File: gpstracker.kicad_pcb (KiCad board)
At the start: 2 copper layers, 75.2 x 54.6 mm, 66 parts, among them IC1 SIM808, J1 Molex 47346-0001, J2 Leds, J3 47553-0001, J4 CONN_COAXIAL, J5 CONN_COAXIAL, J6 Micro_SD_Card, Q1 DMP1045U, SW1 Reset, U1 MCP73832-5-OT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

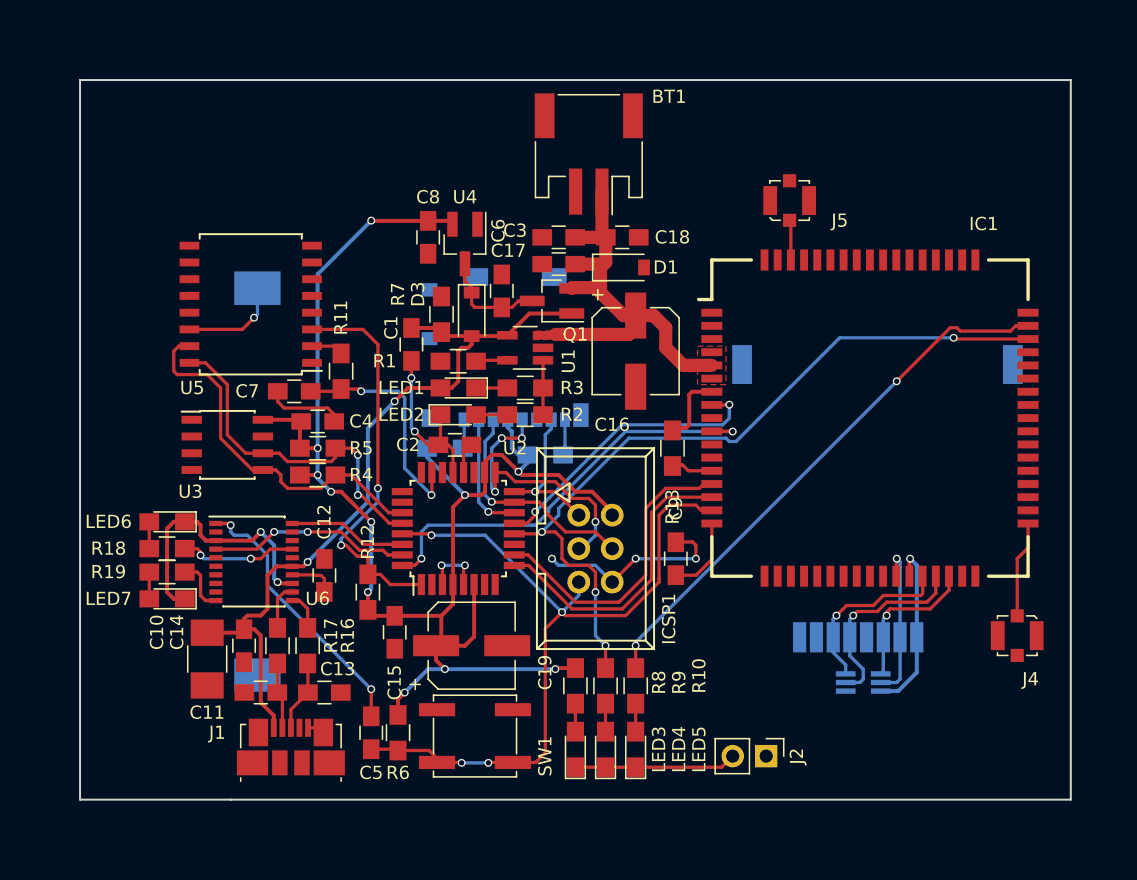
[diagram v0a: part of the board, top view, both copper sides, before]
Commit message: Finished PCB, powering eeprom from arduino
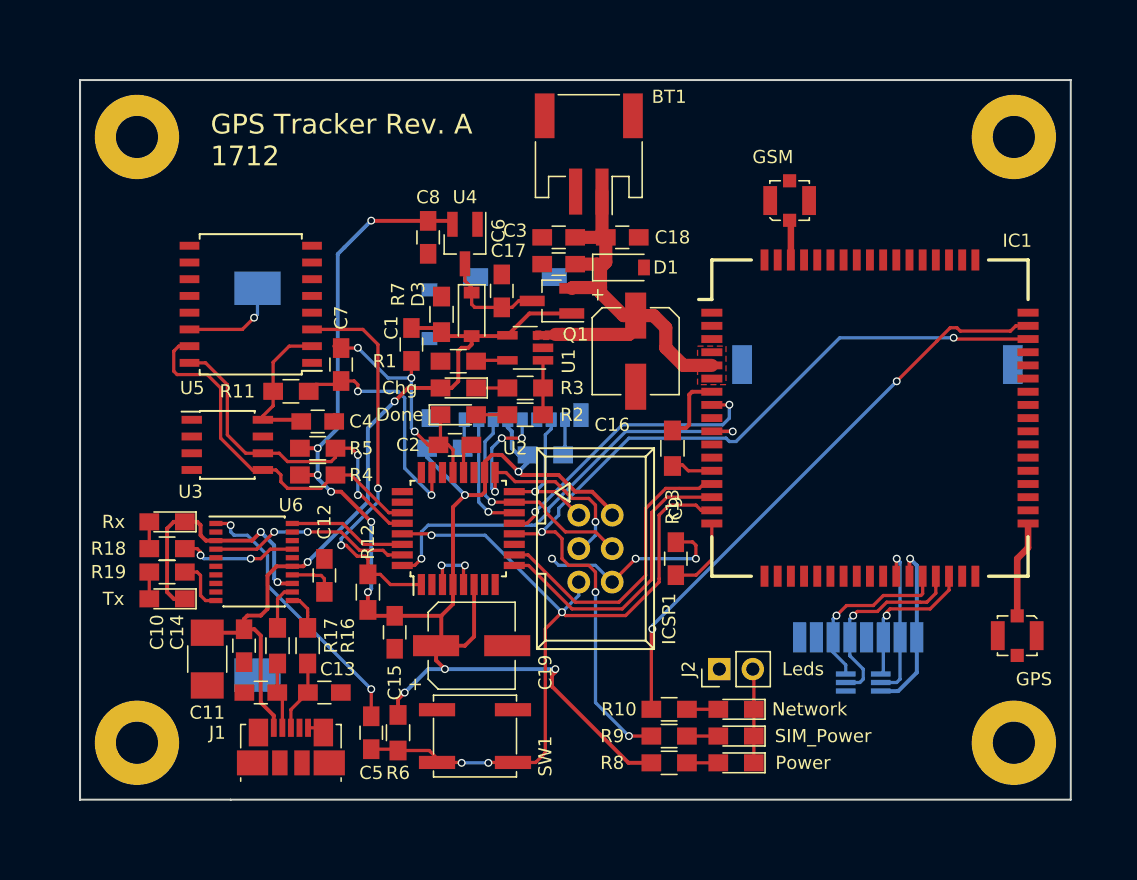
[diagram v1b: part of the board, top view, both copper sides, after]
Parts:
- added REF**: MountingHole_3.2mm_M3_Pad, Mounting_Holes:MountingHole_3.2mm_M3_Pad, F.Cu at (171.7, 118.9)
- added REF**: MountingHole_3.2mm_M3_Pad, Mounting_Holes:MountingHole_3.2mm_M3_Pad, F.Cu at (171.7, 72.9)
- added REF**: MountingHole_3.2mm_M3_Pad, Mounting_Holes:MountingHole_3.2mm_M3_Pad, F.Cu at (105.2, 118.9)
- added REF**: MountingHole_3.2mm_M3_Pad, Mounting_Holes:MountingHole_3.2mm_M3_Pad, F.Cu at (105.2, 72.9)
- moved LED3 12.2 mm to (150.6, 120.4), turned to 180 degrees
- moved LED4 9.96 mm to (150.6, 118.4), turned to 180 degrees
- moved R8 9.20 mm to (145.5, 120.4), turned to 180 degrees
- moved LED5 8.21 mm to (150.6, 116.3), turned to 180 degrees
- moved J2 7.50 mm to (149.4, 113.3), turned to 90 degrees
- moved R9 6.15 mm to (145.5, 118.4), turned to 180 degrees
- moved R11 4.10 mm to (116.8, 92.2), turned to 0 degrees
- moved C7 4.10 mm to (120.7, 90.2), turned to 90 degrees
- moved R10 3.10 mm to (145.5, 116.3), turned to 180 degrees
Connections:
- net Net-(IC1-Pad35) renamed /GPS
- net Net-(IC1-Pad66) renamed /GSM
- C4 pad 1: +3V3 -> +3.3VP
- R11 pad 1: Net-(R11-Pad1) -> +3.3VP
- U3 pad 8: +3V3 -> +3.3VP
- U5 pad 2: Net-(R11-Pad1) -> +3.3VP
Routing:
- net +3.3VP: track 0.00 -> 11.2 mm
- net /SIM808_S: track 59.5 -> 67.1 mm
- net Net-(J2-Pad2): track 12.3 -> 7.15 mm
- net +3V3: track 116.5 -> 121.3 mm
- net /NETWORK_LED: track 41.9 -> 44.5 mm
- net Net-(R11-Pad1): track 2.44 -> 0.00 mm
- net GND: track 52.3 -> 53.9 mm, vias 8 -> 9
- net /RTC_PWR: track 17.4 -> 18.3 mm
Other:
- net class RF added: clearance 0.2, trace_width 0.5, via_dia 0.6, via_drill 0.4
- board text added: "GPS"
- board text added: "GPS Tracker Rev. A 1712"
- board text added: "GSM"

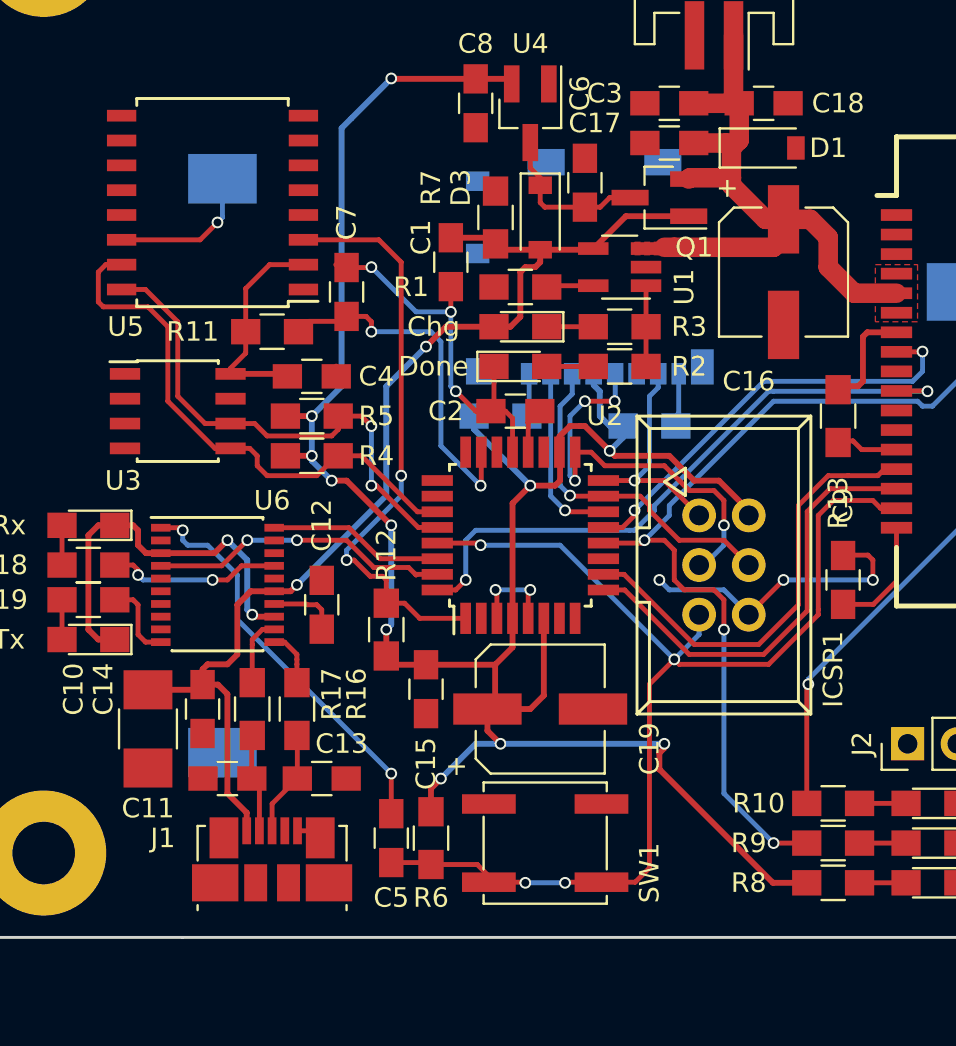
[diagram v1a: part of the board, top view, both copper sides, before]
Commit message: Added via near decoupling capacitors
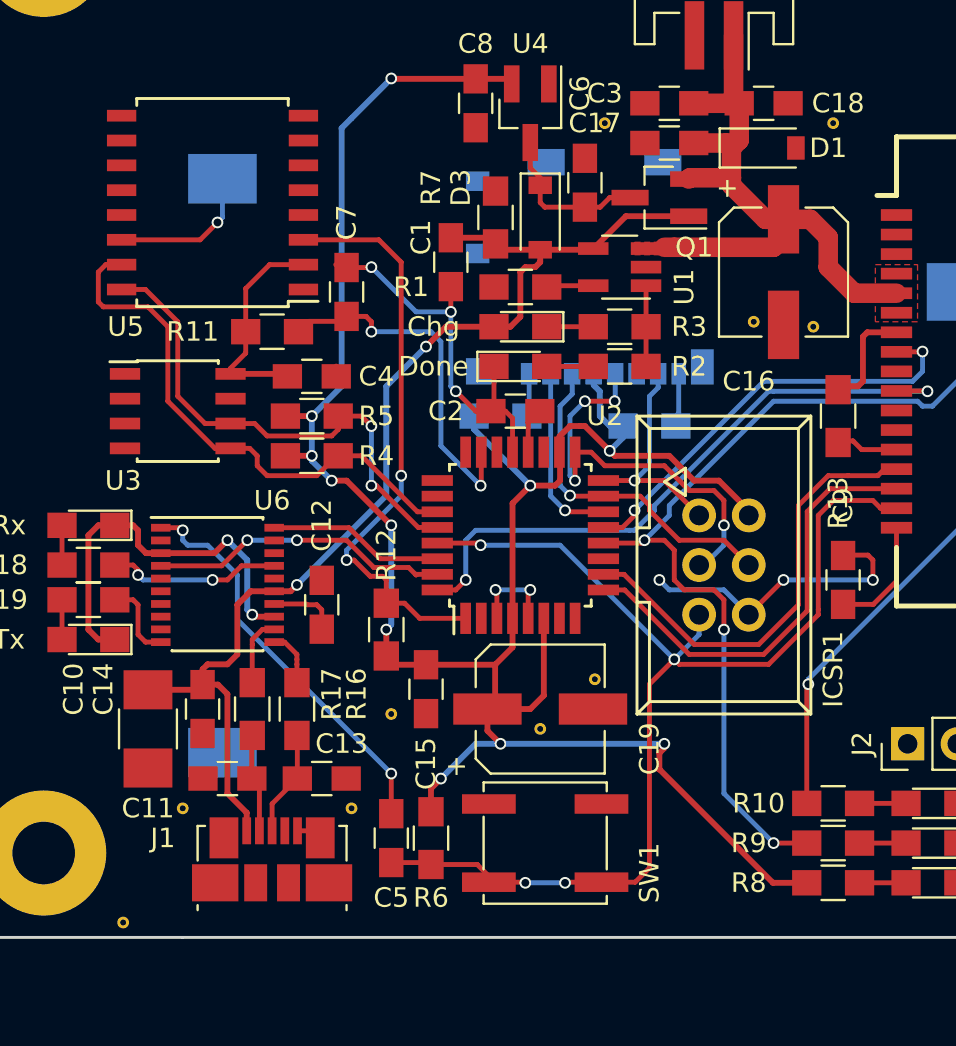
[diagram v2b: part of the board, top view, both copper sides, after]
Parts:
- added VIA**: Via-0.6mm, custom-conn:Via-0.6mm, F.Cu at (109.2, 122.4)
- added VIA**: Via-0.6mm, custom-conn:Via-0.6mm, F.Cu at (141.5, 91.7)
- added VIA**: Via-0.6mm, custom-conn:Via-0.6mm, F.Cu at (120.9, 116.6)
- added VIA**: Via-0.6mm, custom-conn:Via-0.6mm, F.Cu at (112.3, 116.6)
- added VIA**: Via-0.6mm, custom-conn:Via-0.6mm, F.Cu at (145.5, 81.5)
- added VIA**: Via-0.6mm, custom-conn:Via-0.6mm, F.Cu at (133.9, 81.5)
- added VIA**: Via-0.6mm, custom-conn:Via-0.6mm, F.Cu at (122.9, 111.8)
- added VIA**: Via-0.6mm, custom-conn:Via-0.6mm, F.Cu at (130.6, 112.5)
- added VIA**: Via-0.6mm, custom-conn:Via-0.6mm, F.Cu at (133.3, 110.0)
- added VIA**: Via-0.6mm, custom-conn:Via-0.6mm, F.Cu at (144.5, 91.9)
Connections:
- REF** pad 1: (no net) -> GND (x4)
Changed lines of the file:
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@@
-(kicad_pcb (version 4) (host pcbnew 4.0.6)
+(kicad_pcb (version 4) (host pcbnew 4.0.7)
   (general
-    (links 195)
+    (links 209)
     (no_connects 0)
     (area 6.35 7.112 291.084001 205.994001)
@@
     (tracks 611)
     (zones 0)
-    (modules 70)
+    (modules 80)
     (nets 111)
   )
@@
     (mod_text_size 1 1)
     (mod_text_width 0.15)
-    (pad_size 1.6 0.6)
-    (pad_drill 0)
+    (pad_size 6.4 6.4)
+    (pad_drill 3.2)
     (pad_to_mask_clearance 0.2)
     (aux_axis_origin 0 0)
@@
     (add_net /GSM)
   )
+  (module custom-conn:Via-0.6mm (layer F.Cu)
+    (at 109.22 122.428)
+    (fp_text reference VIA** (at 0 1.27) (layer F.SilkS) hide
+      (effects (font (size 1 1) (thickness 0.15)))
+    )
+    (fp_text value Via-0.6mm (at 0 -1.016) (layer F.Fab) hide
+      (effects (font (size 1 1) (thickness 0.15)))
+    )
+    (pad 1 thru_hole circle (at 0 0) (size 0.6 0.6) (drill 0.3) (layers *.Cu)
+      (net 2 GND) (zone_connect 2))
+  )
+  (module custom-conn:Via-0.6mm (layer F.Cu)
+    (at 120.904 116.586)
+    (fp_text reference VIA** (at 0 1.27) (layer F.SilkS) hide
+      (effects (font (size 1 1) (thickness 0.15)))
+    )
+    (fp_text value Via-0.6mm (at 0 -1.016) (layer F.Fab) hide
+      (effects (font (size 1 1) (thickness 0.15)))
+    )
+    (pad 1 thru_hole circle (at 0 0) (size 0.6 0.6) (drill 0.3) (layers *.Cu)
+      (net 2 GND) (zone_connect 2))
+  )
+  (module custom-conn:Via-0.6mm (layer F.Cu)
+    (at 112.268 116.586)
+    (fp_text reference VIA** (at 0 1.27) (layer F.SilkS) hide
+      (effects (font (size 1 1) (thickness 0.15)))
+    )
+    (fp_text value Via-0.6mm (at 0 -1.016) (layer F.Fab) hide
+      (effects (font (size 1 1) (thickness 0.15)))
+    )
+    (pad 1 thru_hole circle (at 0 0) (size 0.6 0.6) (drill 0.3) (layers *.Cu)
+      (net 2 GND) (zone_connect 2))
+  )
+  (module custom-conn:Via-0.6mm (layer F.Cu)
+    (at 145.542 81.534)
+    (fp_text reference VIA** (at 0 1.27) (layer F.SilkS) hide
+      (effects (font (size 1 1) (thickness 0.15)))
+    )
+    (fp_text value Via-0.6mm (at 0 -1.016) (layer F.Fab) hide
+      (effects (font (size 1 1) (thickness 0.15)))
+    )
+    (pad 1 thru_hole circle (at 0 0) (size 0.6 0.6) (drill 0.3) (layers *.Cu)
+      (net 2 GND) (zone_connect 2))
+  )
+  (module custom-conn:Via-0.6mm (layer F.Cu)
+    (at 133.858 81.534)
+    (fp_text reference VIA** (at 0 1.27) (layer F.SilkS) hide
+      (effects (font (size 1 1) (thickness 0.15)))
+    )
+    (fp_text value Via-0.6mm (at 0 -1.016) (layer F.Fab) hide
+      (effects (font (size 1 1) (thickness 0.15)))
+    )
+    (pad 1 thru_hole circle (at 0 0) (size 0.6 0.6) (drill 0.3) (layers *.Cu)
+      (net 2 GND) (zone_connect 2))
+  )
+  (module custom-conn:Via-0.6mm (layer F.Cu)
+    (at 122.936 111.76)
+    (fp_text reference VIA** (at 0 1.27) (layer F.SilkS) hide
+      (effects (font (size 1 1) (thickness 0.15)))
+    )
+    (fp_text value Via-0.6mm (at 0 -1.016) (layer F.Fab) hide
+      (effects (font (size 1 1) (thickness 0.15)))
+    )
+    (pad 1 thru_hole circle (at 0 0) (size 0.6 0.6) (drill 0.3) (layers *.Cu)
+      (net 2 GND) (zone_connect 2))
+  )
+  (module custom-conn:Via-0.6mm (layer F.Cu)
+    (at 130.556 112.522)
+    (fp_text reference VIA** (at 0 1.27) (layer F.SilkS) hide
+      (effects (font (size 1 1) (thickness 0.15)))
+    )
+    (fp_text value Via-0.6mm (at 0 -1.016) (layer F.Fab) hide
+      (effects (font (size 1 1) (thickness 0.15)))
+    )
+    (pad 1 thru_hole circle (at 0 0) (size 0.6 0.6) (drill 0.3) (layers *.Cu)
+      (net 2 GND) (zone_connect 2))
+  )
+  (module custom-conn:Via-0.6mm (layer F.Cu)
+    (at 133.35 109.982)
+    (fp_text reference VIA** (at 0 1.27) (layer F.SilkS) hide
+      (effects (font (size 1 1) (thickness 0.15)))
+    )
+    (fp_text value Via-0.6mm (at 0 -1.016) (layer F.Fab) hide
+      (effects (font (size 1 1) (thickness 0.15)))
+    )
+    (pad 1 thru_hole circle (at 0 0) (size 0.6 0.6) (drill 0.3) (layers *.Cu)
+      (net 2 GND) (zone_connect 2))
+  )
+  (module custom-conn:Via-0.6mm (layer F.Cu)
+    (at 144.526 91.948)
+    (fp_text reference VIA** (at 0 1.27) (layer F.SilkS) hide
+      (effects (font (size 1 1) (thickness 0.15)))
+    )
+    (fp_text value Via-0.6mm (at 0 -1.016) (layer F.Fab) hide
+      (effects (font (size 1 1) (thickness 0.15)))
+    )
+    (pad 1 thru_hole circle (at 0 0) (size 0.6 0.6) (drill 0.3) (layers *.Cu)
+      (net 2 GND) (zone_connect 2))
+  )
   (module Mounting_Holes:MountingHole_3.2mm_M3_Pad (layer F.Cu)
     (at 171.704 118.872)
@@
     (fp_circle (center 0 0) (end 3.2 0) (layer Cmts.User) (width 0.15))
     (fp_circle (center 0 0) (end 3.45 0) (layer F.CrtYd) (width 0.05))
-    (pad 1 thru_hole circle (at 0 0) (size 6.4 6.4) (drill 3.2) (layers *.Cu *.Mask))
+    (pad 1 thru_hole circle (at 0 0) (size 6.4 6.4) (drill 3.2) (layers *.Cu *.Mask)
+      (net 2 GND))
   )
   (module Mounting_Holes:MountingHole_3.2mm_M3_Pad (layer F.Cu)
@@
     (fp_circle (center 0 0) (end 3.2 0) (layer Cmts.User) (width 0.15))
     (fp_circle (center 0 0) (end 3.45 0) (layer F.CrtYd) (width 0.05))
-    (pad 1 thru_hole circle (at 0 0) (size 6.4 6.4) (drill 3.2) (layers *.Cu *.Mask))
+    (pad 1 thru_hole circle (at 0 0) (size 6.4 6.4) (drill 3.2) (layers *.Cu *.Mask)
+      (net 2 GND))
   )
   (module Mounting_Holes:MountingHole_3.2mm_M3_Pad (layer F.Cu)
@@
     (fp_circle (center 0 0) (end 3.2 0) (layer Cmts.User) (width 0.15))
     (fp_circle (center 0 0) (end 3.45 0) (layer F.CrtYd) (width 0.05))
-    (pad 1 thru_hole circle (at 0 0) (size 6.4 6.4) (drill 3.2) (layers *.Cu *.Mask))
+    (pad 1 thru_hole circle (at 0 0) (size 6.4 6.4) (drill 3.2) (layers *.Cu *.Mask)
+      (net 2 GND))
   )
   (module 104031-0811:MOLEX_104031-0811 (layer B.Cu)
@@
     (fp_circle (center 0 0) (end 3.2 0) (layer Cmts.User) (width 0.15))
     (fp_circle (center 0 0) (end 3.45 0) (layer F.CrtYd) (width 0.05))
-    (pad 1 thru_hole circle (at 0 0) (size 6.4 6.4) (drill 3.2) (layers *.Cu *.Mask))
+    (pad 1 thru_hole circle (at 0 0) (size 6.4 6.4) (drill 3.2) (layers *.Cu *.Mask)
+      (net 2 GND))
+  )
+  (module custom-conn:Via-0.6mm (layer F.Cu)
+    (at 141.478 91.694)
+    (fp_text reference VIA** (at 0 1.27) (layer F.SilkS) hide
+      (effects (font (size 1 1) (thickness 0.15)))
+    )
+    (fp_text value Via-0.6mm (at 0 -1.016) (layer F.Fab) hide
+      (effects (font (size 1 1) (thickness 0.15)))
+    )
+    (pad 1 thru_hole circle (at 0 0) (size 0.6 0.6) (drill 0.3) (layers *.Cu)
+      (net 2 GND) (zone_connect 2))
   )
   (gr_text GSM (at 153.416 74.422) (layer F.SilkS)
